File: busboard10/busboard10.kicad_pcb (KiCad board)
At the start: 2 copper layers, 200 x 25 mm, 28 parts, among them J1 Synth_power_2x5_narrow, J10 Synth_power_2x5_narrow, J11 Synth_power_2x5_narrow, J12 Synth_power_2x5_narrow, J13 Conn_01x03, J2 Synth_power_2x5_narrow, J3 Synth_power_2x5_narrow, J4 Synth_power_2x5_narrow, J5 Synth_power_2x5_narrow, J6 Synth_power_2x5_narrow, J7 Synth_power_2x5_narrow, J8 Synth_power_2x5_narrow, J9 Synth_power_2x5_narrow

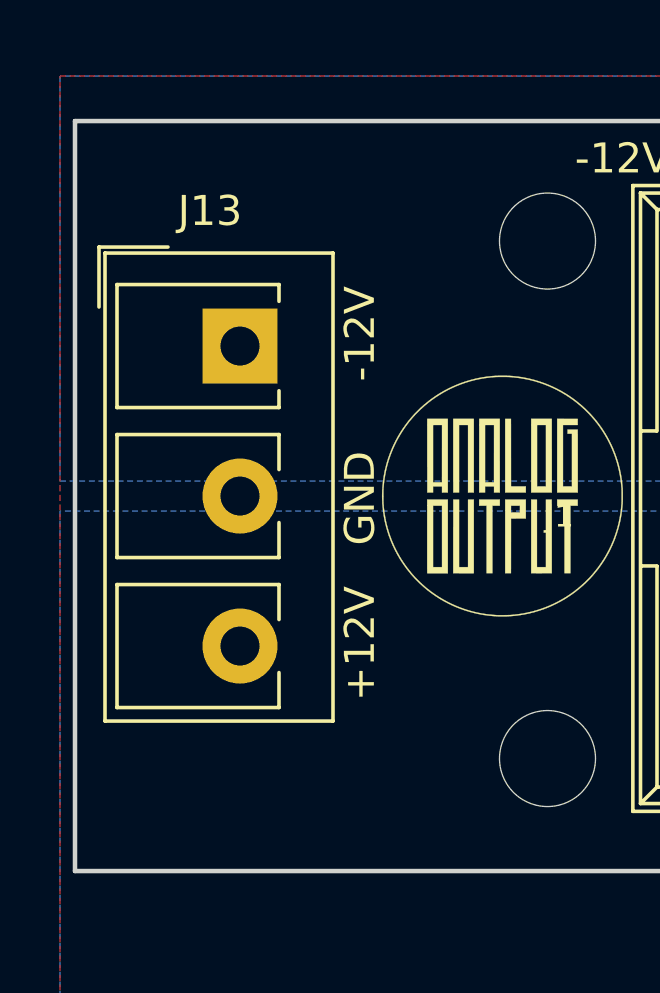
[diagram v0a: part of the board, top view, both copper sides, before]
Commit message: Correct orientation of terminal block
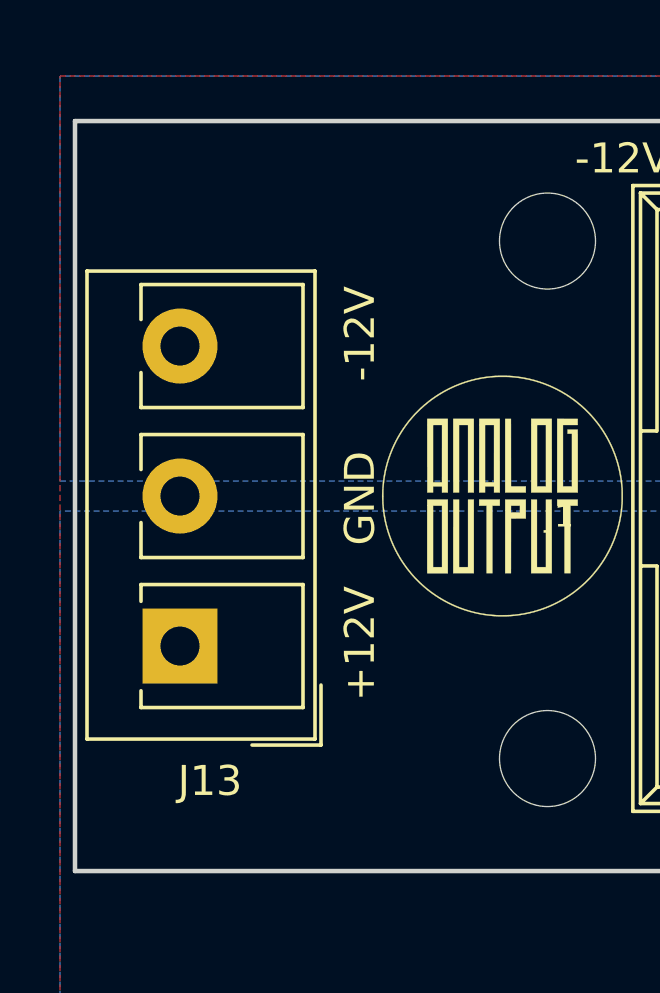
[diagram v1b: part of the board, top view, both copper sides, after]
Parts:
- moved J13 2.00 mm to (45.5, 62.5), turned to 90 degrees
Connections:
- J13 pad 1: -12V -> +12V
- J13 pad 3: +12V -> -12V

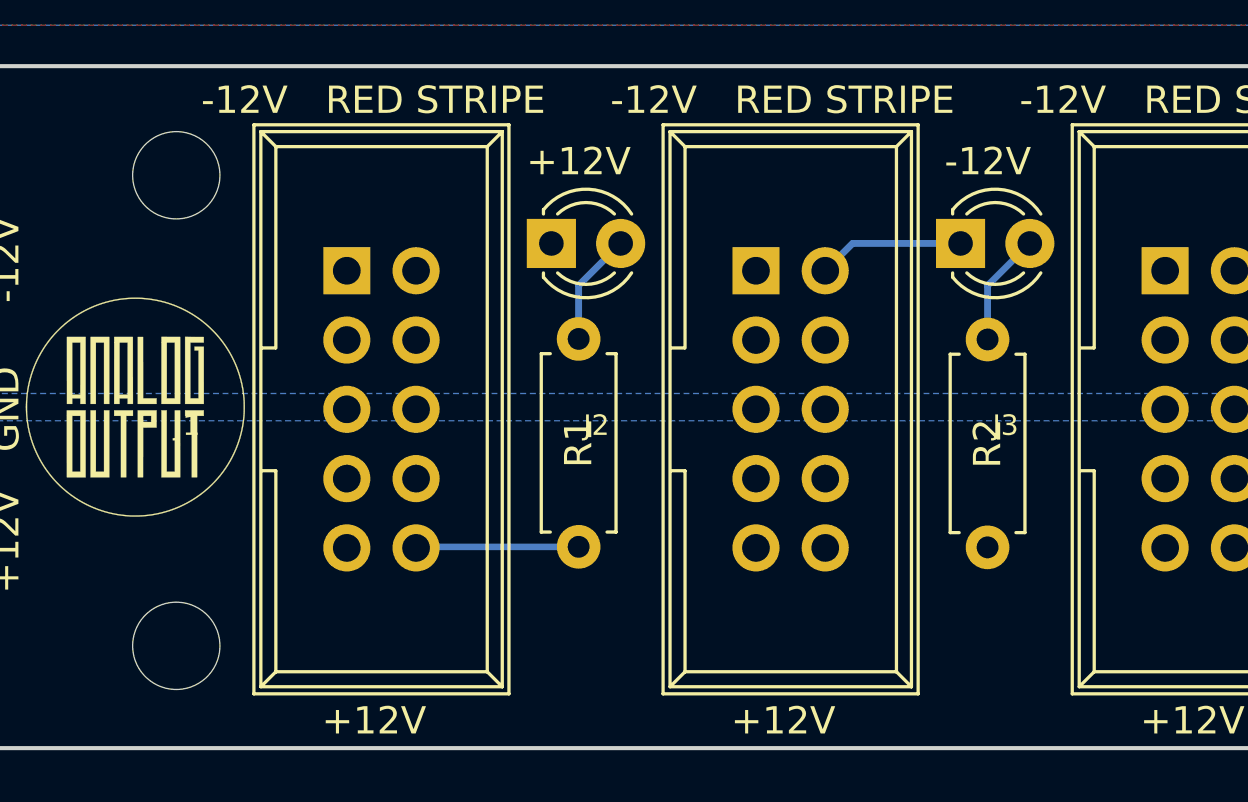
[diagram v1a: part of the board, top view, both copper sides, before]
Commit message: Changed resistor footprint
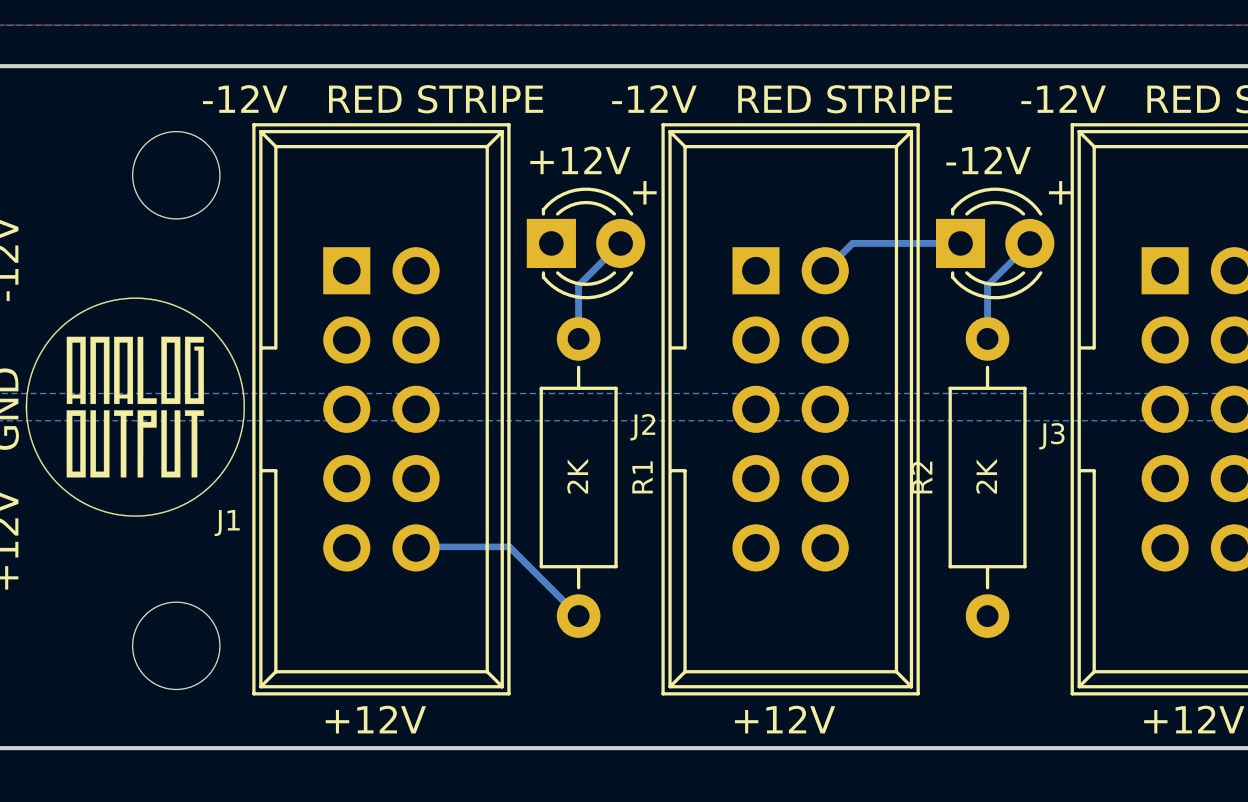
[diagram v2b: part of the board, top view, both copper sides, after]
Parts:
- R1, R2: footprint Resistor_THT:R_Axial_DIN0207_L6.3mm_D2.5mm_P7.62mm_Horizontal -> ao_tht:R_Axial_DIN0207_L6.3mm_D2.5mm_P10.16mm_Horizontal
- moved R2 2.52 mm to (87.5, 70.2)
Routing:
- net +12V: track 6.06 -> 7.11 mm
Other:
- rule pad_to_mask_clearance: 0.051 -> 0
- board text added: "+"
